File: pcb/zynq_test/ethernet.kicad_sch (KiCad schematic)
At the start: 61 parts, among them J1101 RJ45_JK0654219, Q1101 FDY102PZ, Q1102 2N7002E, Q1103 2N7002E, U1101 DSC1001CI2-025, U1102 LAN8830

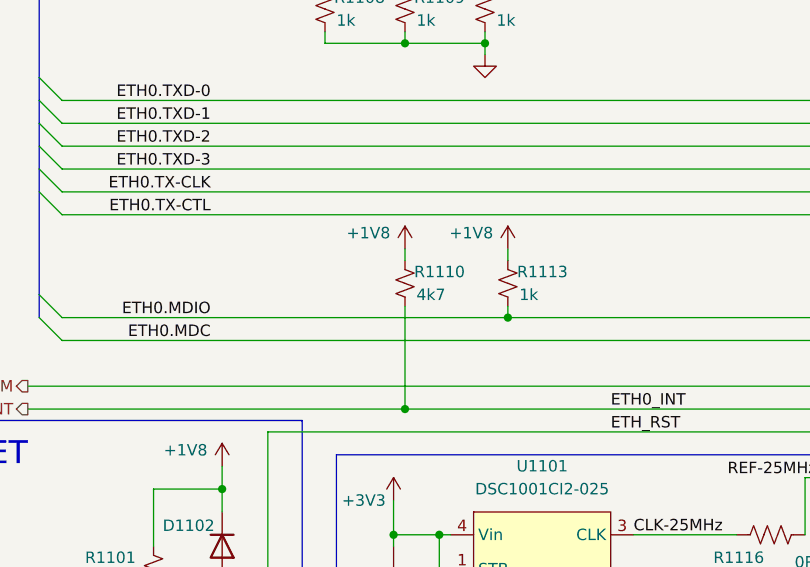
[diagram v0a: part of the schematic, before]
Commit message: finished diff of HDMI
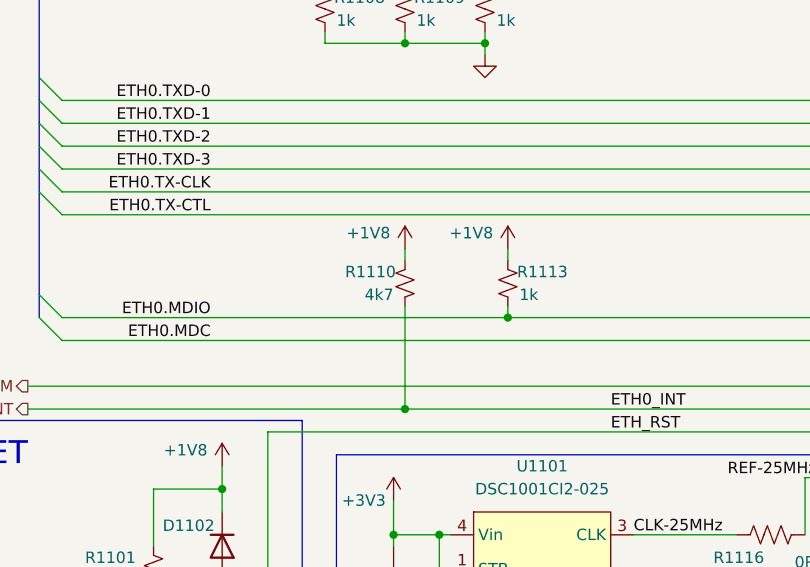
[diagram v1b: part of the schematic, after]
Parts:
- R1102, R1103, R1104, R1105, R1106, R1107, R1108, R1109, R1110, R1111, R1112, R1113, R1114, R1115: footprint (none) -> Resistor_SMD:R_0402_1005Metric
- U1101: footprint (none) -> other:DSC1001
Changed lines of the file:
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@@
 			)
 		)
-		(property "Footprint" ""
+		(property "Footprint" "other:DSC1001"
 			(at 85.09 114.3 0)
 			(effects
@@
 		(lib_id "Device:R_Small_US")
 		(at 69.85 82.55 0)
+		(mirror y)
 		(unit 1)
 		(exclude_from_sim no)
@@
 		(dnp no)
 		(property "Reference" "R1110"
-			(at 70.866 81.28 0)
+			(at 68.834 81.28 0)
 			(effects
 				(font
@@
 		)
 		(property "Value" "4k7"
-			(at 71.12 83.82 0)
+			(at 68.58 83.82 0)
 			(effects
 				(font
@@
 			)
 		)
-		(property "Footprint" ""
+		(property "Footprint" "Resistor_SMD:R_0402_1005Metric"
 			(at 69.85 82.55 0)
 			(effects
@@
 			)
 		)
-		(property "Footprint" ""
+		(property "Footprint" "Resistor_SMD:R_0402_1005Metric"
 			(at 52.07 40.64 0)
 			(effects
@@
 			)
 		)
-		(property "Footprint" ""
+		(property "Footprint" "Resistor_SMD:R_0402_1005Metric"
 			(at 52.07 38.1 0)
 			(effects
@@
 			)
 		)
-		(property "Footprint" ""
+		(property "Footprint" "Resistor_SMD:R_0402_1005Metric"
 			(at 81.28 29.21 0)
 			(effects
@@
 			)
 		)
-		(property "Footprint" ""
+		(property "Footprint" "Resistor_SMD:R_0402_1005Metric"
 			(at 52.07 45.72 0)
 			(effects
@@
 			)
 		)
-		(property "Footprint" ""
+		(property "Footprint" "Resistor_SMD:R_0402_1005Metric"
 			(at 60.96 52.07 0)
 			(effects
@@
 			)
 		)
-		(property "Footprint" ""
+		(property "Footprint" "Resistor_SMD:R_0402_1005Metric"
 			(at 52.07 35.56 0)
 			(effects
@@
 			)
 		)
-		(property "Footprint" ""
+		(property "Footprint" "Resistor_SMD:R_0402_1005Metric"
 			(at 52.07 43.18 0)
 			(effects
@@
 			)
 		)
-		(property "Footprint" ""
+		(property "Footprint" "Resistor_SMD:R_0402_1005Metric"
 			(at 81.28 82.55 0)
 			(effects
@@
 			)
 		)
-		(property "Footprint" ""
+		(property "Footprint" "Resistor_SMD:R_0402_1005Metric"
 			(at 90.17 29.21 0)
 			(effects
@@
 			)
 		)
-		(property "Footprint" ""
+		(property "Footprint" "Resistor_SMD:R_0402_1005Metric"
 			(at 78.74 52.07 0)
 			(effects
@@
 			)
 		)
-		(property "Footprint" ""
+		(property "Footprint" "Resistor_SMD:R_0402_1005Metric"
 			(at 97.79 30.48 0)
 			(effects
@@
 			)
 		)
-		(property "Footprint" ""
+		(property "Footprint" "Resistor_SMD:R_0402_1005Metric"
 			(at 69.85 52.07 0)
 			(effects
@@
 			)
 		)
-		(property "Footprint" ""
+		(property "Footprint" "Resistor_SMD:R_0402_1005Metric"
 			(at 52.07 48.26 0)
 			(effects

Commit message: Almost done with BOM
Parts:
- C1101, C1103, C1105, C1113, C1118, C1122: footprint (none) -> Capacitor_SMD:C_0805_2012Metric
- C1102, C1104, C1106, C1107, C1108, C1109, C1110, C1111, C1112, C1114, C1115, C1116, C1117, C1121: footprint (none) -> Capacitor_SMD:C_0402_1005Metric
- C1119, C1120: footprint (none) -> Capacitor_SMD:C_1210_3225Metric
- D1101, D1102: footprint (none) -> Diode_SMD:D_SOD-123
- L1101, L1102: footprint (none) -> Capacitor_SMD:C_0603_1608Metric
- Q1101: footprint (none) -> other:SC-89-3
- R1101, R1116, R1117, R1118, R1121, R1122, R1123, R1124: footprint (none) -> Resistor_SMD:R_0402_1005Metric
- R1119: renamed from R1120; footprint (none) -> Resistor_SMD:R_0402_1005Metric
- R1120: renamed from R1119; footprint (none) -> Resistor_SMD:R_0402_1005Metric
- R1125: renamed from R1129; footprint (none) -> Resistor_SMD:R_0805_2012Metric
- R1126: renamed from R1125; footprint (none) -> Resistor_SMD:R_0402_1005Metric
- R1127: renamed from R1126; footprint (none) -> Resistor_SMD:R_0402_1005Metric
- R1128: renamed from R1127; footprint (none) -> Resistor_SMD:R_0402_1005Metric; now not fitted
- R1129: renamed from R1128; footprint (none) -> Resistor_SMD:R_0402_1005Metric
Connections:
- net +1V8: now also C1107.1, U1101.1 (STB), U1101.4 (Vin)
- net +3V3: now also Q1101.2 (S); no longer C1107.1, Q1101.3 (S), U1101.1 (STB), U1101.4 (Vin)
- net ETH_1V1: now also Q1101.3 (D); no longer Q1101.1 (D)
- net ETH_LDO: now also Q1101.1 (G); no longer Q1101.2 (G)
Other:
- moved on the sheet: C1122, Q1103, R1121, R1122, R1123, R1124, R1125, R1126, R1127, R1129

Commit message: Version sent to JLCPCB
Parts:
- C1101, C1103, C1105, C1113, C1118: JLCPCB Part# (none) -> C15850; PART_NUMBER (none) -> CL21A106KAYNNNE
- C1102, C1104, C1106, C1107, C1108, C1109, C1110, C1112, C1114, C1115, C1117, C1121: JLCPCB Part# (none) -> C1525; PART_NUMBER (none) -> CL05B104KO5NNNC
- C1111: JLCPCB Part# (none) -> C77013; PART_NUMBER (none) -> GRM155R71E103KA01D
- C1116: JLCPCB Part# (none) -> C23733; PART_NUMBER (none) -> CL05A475MP5NRNC
- C1119, C1120: JLCPCB Part# (none) -> C525654; PART_NUMBER (none) -> CL32A476KPJNNNE
- C1122: JLCPCB Part# (none) -> C440004; PART_NUMBER (none) -> FM21X102K501PXG
- D1101, D1102: JLCPCB Part# (none) -> C2099; PART_NUMBER (none) -> 1N4148W
- J1101: JLCPCB Part# (none) -> C3179230; PART_NUMBER (none) -> ARJM11C7-502-AB-ER2-T
- L1101, L1102: JLCPCB Part# (none) -> C5120901; PART_NUMBER (none) -> 742792023
- Q1101: JLCPCB Part# (none) -> C467787; PART_NUMBER (none) -> FDY102PZ
- Q1102, Q1103: JLCPCB Part# (none) -> C71533; PART_NUMBER (none) -> 2N7002E
- R1101: JLCPCB Part# (none) -> C191123; PART_NUMBER (none) -> ERJ2RKF1002X
- R1102, R1103, R1104, R1105, R1106, R1107: JLCPCB Part# (none) -> C264051; PART_NUMBER (none) -> ERJ2GEJ330X
- R1108, R1109, R1111, R1112, R1113, R1114, R1115, R1121, R1123, R1124, R1126, R1129: JLCPCB Part# (none) -> C242161; PART_NUMBER (none) -> ERJ2RKF1001X
- R1110: JLCPCB Part# (none) -> C327817; PART_NUMBER (none) -> MR04X4701FTL
- R1116, R1119, R1120: JLCPCB Part# (none) -> C242160; PART_NUMBER (none) -> ERJ2GE0R00X
- R1117: JLCPCB Part# (none) -> C192169; PART_NUMBER (none) -> ERJ2RKF1003X
- R1118: JLCPCB Part# (none) -> C416563; PART_NUMBER (none) -> ERJ2RKF6041X
- R1122, R1127: JLCPCB Part# (none) -> C412979; PART_NUMBER (none) -> ERJ2GEJ221X
- R1125: JLCPCB Part# (none) -> C17514; PART_NUMBER (none) -> 0805W8F1004T5E
- U1101: JLCPCB Part# (none) -> C611667; PART_NUMBER (none) -> DSC1001CI2-025.0000T
- U1102: JLCPCB Part# (none) -> C6285537; PART_NUMBER (none) -> LAN8830-V/PSA
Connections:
- net +1V8: no longer C1107.1, U1101.1 (STB), U1101.4 (Vin)
- net +3V3: now also C1107.1, U1101.1 (STB), U1101.4 (Vin)
- net REF-25MHz: now also U1102.46 (XI); no longer U1102.45 (XO)
